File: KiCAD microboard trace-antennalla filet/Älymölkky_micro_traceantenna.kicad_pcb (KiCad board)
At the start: 2 copper layers, 57.2 x 21.1 mm, 43 parts, among them U1 nRF52810-QCxx, X1 32MHz Crystal, X1_C1 12pF, X1_C2 12pF, X2 32.768 kHz Crystal, X2_C11 12pF, X2_C12 12pF

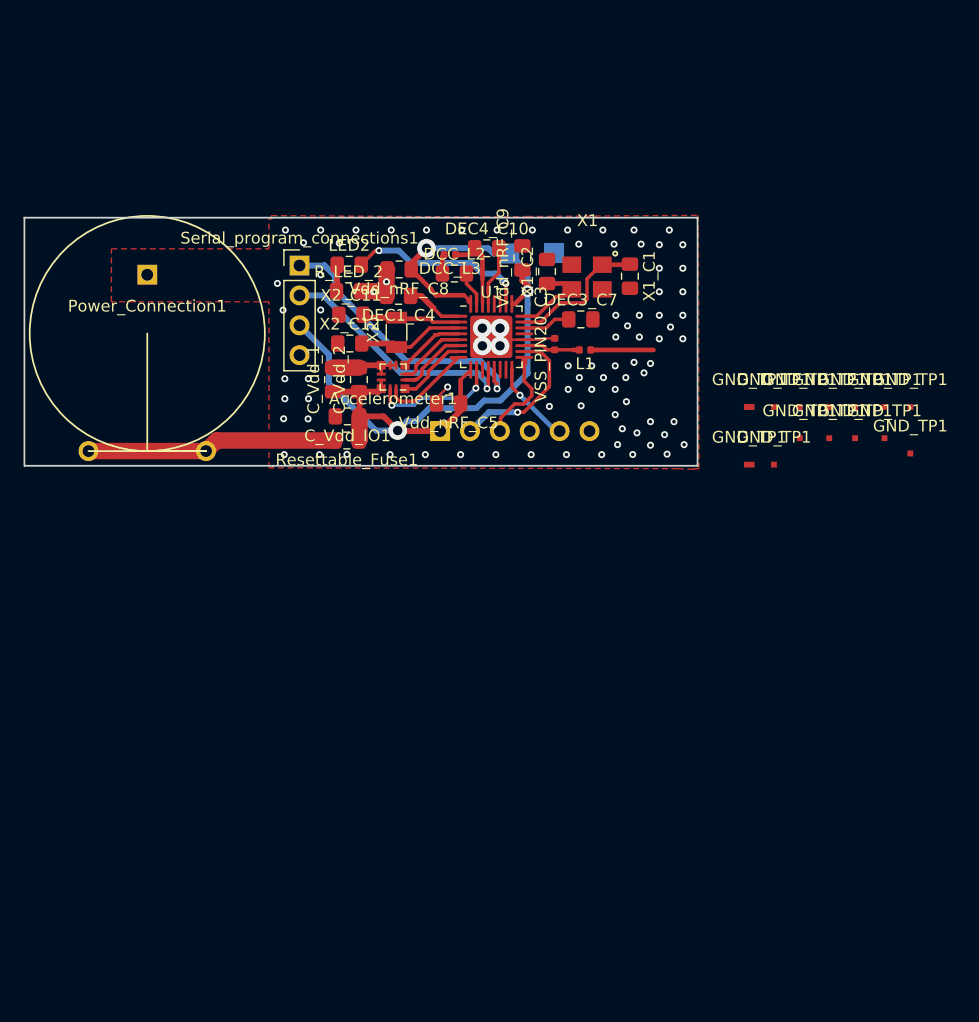
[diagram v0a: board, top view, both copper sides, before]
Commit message: Readymade design with antenna, only antenna connection not wide enough, needs 3mm
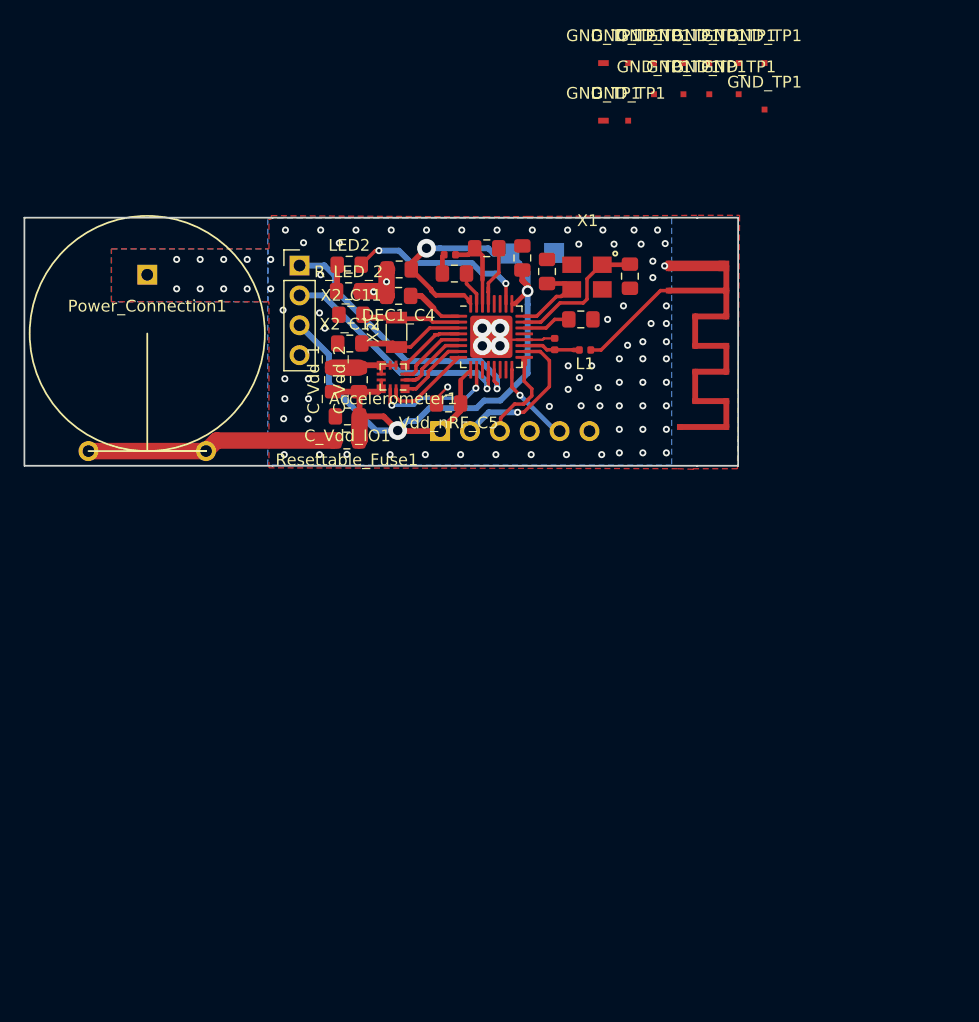
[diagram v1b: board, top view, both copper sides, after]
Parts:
- added ?: Conn_01x01_Male, Custom_footprints_alymolkky:antenna_building_block, F.Cu at (150.8, 92.2)
- added ?: Conn_01x01_Male, Custom_footprints_alymolkky:antenna_building_block, F.Cu at (148.2, 92.2)
- added ?: Conn_01x01_Male, Custom_footprints_alymolkky:antenna_building_block, F.Cu at (150.6, 88.0)
- added ?: Conn_01x01_Male, Custom_footprints_alymolkky:antenna_building_block, F.Cu at (150.8, 101.7)
- added ?: Conn_01x01_Male, Custom_footprints_alymolkky:antenna_building_block, F.Cu at (150.8, 90.0)
- added ?: Conn_01x01_Male, Custom_footprints_alymolkky:antenna_building_block, F.Cu at (148.2, 99.5)
- added ?: Conn_01x01_Male, Custom_footprints_alymolkky:antenna_building_block, F.Cu at (145.9, 88.0)
- added ?: Conn_01x01_Male, Custom_footprints_alymolkky:antenna_building_block, F.Cu at (148.2, 97.0)
- added ?: Conn_01x01_Male, Custom_footprints_alymolkky:antenna_building_block, F.Cu at (145.9, 90.0)
- added ?: Conn_01x01_Male, Custom_footprints_alymolkky:antenna_building_block, F.Cu at (150.8, 94.8)
- added ?: Conn_01x01_Male, Custom_footprints_alymolkky:antenna_building_block, F.Cu at (146.8, 101.7)
- added ?: Conn_01x01_Male, Custom_footprints_alymolkky:antenna_building_block, F.Cu at (150.8, 97.0)
- added ?: Conn_01x01_Male, Custom_footprints_alymolkky:antenna_building_block, F.Cu at (148.2, 94.8)
- added ?: Conn_01x01_Male, Custom_footprints_alymolkky:antenna_building_block, F.Cu at (150.8, 99.5)
- moved GND_TP1 31.8 mm to (140.3, 75.6)
- moved GND_TP1 31.8 mm to (149.3, 70.7)
- moved GND_TP1 31.8 mm to (147.2, 70.7)
- moved GND_TP1 31.8 mm to (147.2, 73.3)
- moved GND_TP1 31.8 mm to (144.7, 73.3)
- moved GND_TP1 31.8 mm to (144.7, 70.7)
- moved GND_TP1 31.8 mm to (140.3, 70.7)
- moved GND_TP1 31.8 mm to (142.4, 75.6)
- moved GND_TP1 31.8 mm to (142.4, 70.7)
- moved GND_TP1 31.8 mm to (151.8, 70.7)
- moved GND_TP1 31.8 mm to (151.8, 73.3)
- moved GND_TP1 31.8 mm to (149.3, 73.3)
- moved GND_TP1 31.8 mm to (154.1, 74.7)
- moved GND_TP1 31.8 mm to (154.1, 70.7)
- renumbered U1 to ?, DCC_L2 to ?, DEC3_C7 to ?, DEC4_C10 to ?, Vdd_nRF_C8 to ?, Vdd_nRF_C9 to ?, VSS_PIN20_C3 to ?, X1_C1 to ?, X1_C2 to ?, DCC_L3 to ?, Serial_program_connections1 to ?
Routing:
- net Earth: track 29.4 -> 70.7 mm, vias 86 -> 89
- added copper zone on B.Cu, net Earth
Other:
- board size 57.2 x 21.1 mm -> 60.7 x 21.1 mm
- board text added: "ÄlyMölkky"

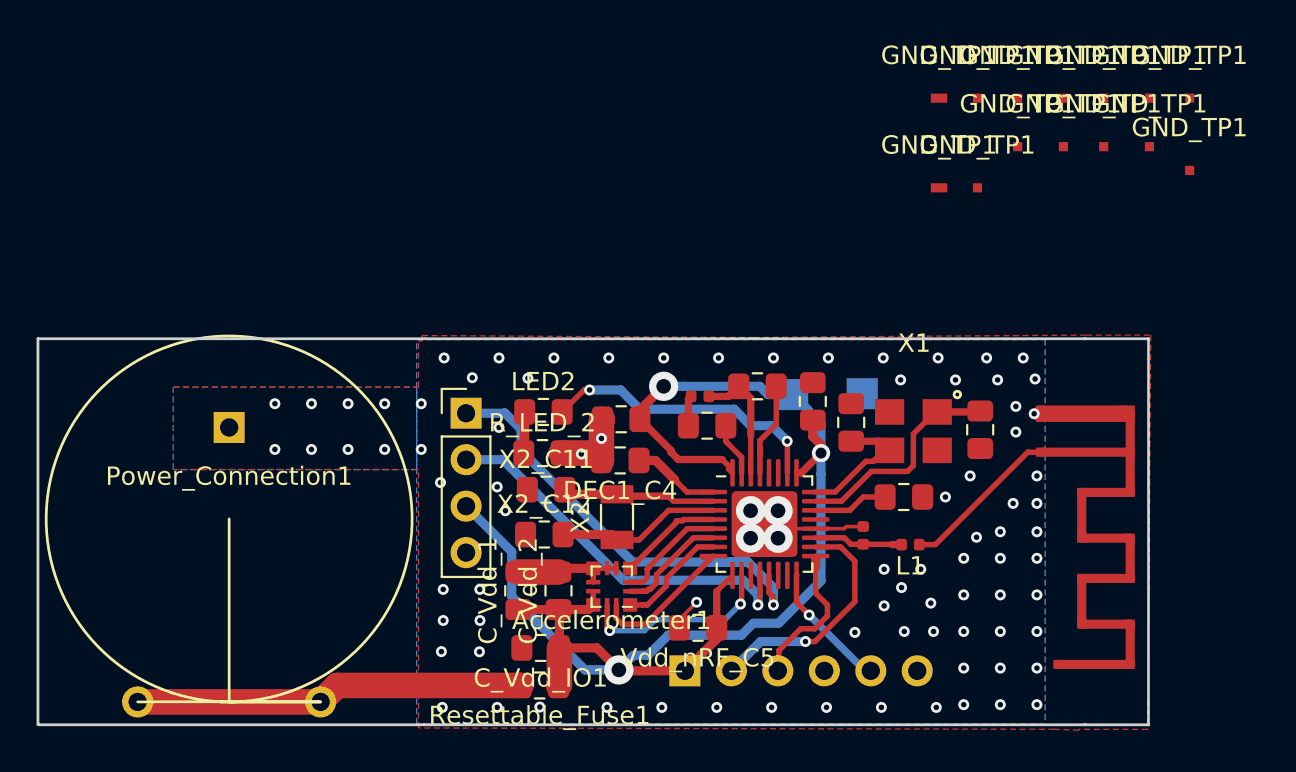
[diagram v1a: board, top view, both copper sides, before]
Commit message: Trace antenna design completed, modifying for order
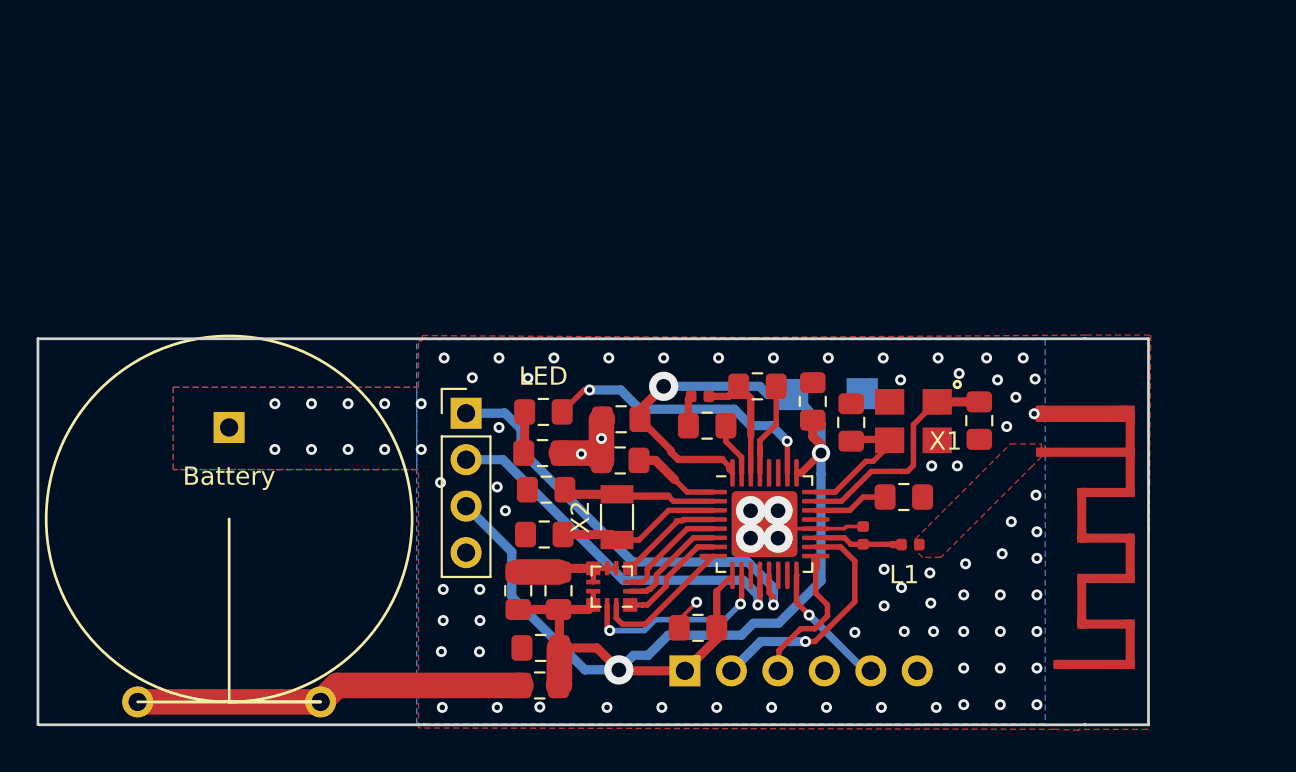
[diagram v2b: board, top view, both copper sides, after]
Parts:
- removed GND_TP1 (x14): Conn_01x01_Male, Custom_footprints_alymolkky:antenna_building_block
- moved X1 0.55 mm to (138.9, 88.3)
- moved ? 0.50 mm to (142.6, 88.3)
- renumbered SWD_connections1 to ?, Accelerometer1 to ?, C_Vdd_1 to ?, C_Vdd_2 to ?, C_Vdd_IO1 to ?, DEC1_C4 to ?, R_LED_2 to ?, Vdd_nRF_C5 to ?, Resettable_Fuse1 to ?, X2_C11 to ?, X2_C12 to ?, Power_Connection1 to Battery, GND_TP1 to GND_TP, LED2 to LED
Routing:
- net Earth: track 70.7 -> 62.0 mm, vias 89 -> 86
- net Net-(U1-Pad23): track 12.0 -> 12.5 mm
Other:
- board text added: "ÄlyMölkky v2.2 Micro with trace"
- board text removed: "ÄlyMölkky"

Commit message: Order ready trace antenna design
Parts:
- added ?: Conn_01x01_Male, Custom_footprints_alymolkky:antenna_building_block, F.Cu at (150.8, 139.8)
- added ?: Conn_01x01_Male, Custom_footprints_alymolkky:antenna_building_block, F.Cu at (150.8, 146.7)
- added ?: Conn_01x01_Male, Custom_footprints_alymolkky:antenna_building_block, F.Cu at (150.8, 135.1)
- added ?: Conn_01x01_Male, Custom_footprints_alymolkky:antenna_building_block, F.Cu at (148.2, 144.4)
- added ?: Conn_01x01_Male, Custom_footprints_alymolkky:antenna_building_block, F.Cu at (150.8, 141.9)
- added ?: Conn_01x01_Male, Custom_footprints_alymolkky:antenna_building_block, F.Cu at (146.8, 146.7)
- added ?: 100nF, Capacitor_SMD:C_0805_2012Metric_Pad1.15x1.40mm_HandSolder, F.Cu at (118.6, 145.8)
- added ?: 100uF, Capacitor_SMD:C_0805_2012Metric_Pad1.15x1.40mm_HandSolder, F.Cu at (117.3, 142.6)
- added ?: Conn_01x06_Male, Connector_PinHeader_2.54mm:PinHeader_1x06_P2.54mm_Vertical, B.Cu at (126.5, 147.0)
- added ?: LIS2DE12, Custom_footprints_alymolkky:LGA-12_2x2mm_P0.5mm, F.Cu at (122.5, 142.4)
- added ?: nRF52810-QCxx, Custom_footprints_alymolkky:QFN-32-1EP_5x5mm_P0.5mm_EP3.6x3.6mm, F.Cu at (130.8, 139.0)
- added ?: Conn_01x01_Male, Custom_footprints_alymolkky:antenna_building_block, F.Cu at (148.2, 137.2)
- added ?: 100nF, Capacitor_SMD:C_0805_2012Metric_Pad1.15x1.40mm_HandSolder, F.Cu at (122.9, 135.5)
- added ?: 10uH, Capacitor_SMD:C_0805_2012Metric_Pad1.15x1.40mm_HandSolder, F.Cu at (127.7, 133.6)
- added ?: 10uF, Capacitor_SMD:C_0805_2012Metric_Pad1.15x1.40mm_HandSolder, F.Cu at (119.5, 142.6)
- added ?: Polyfuse, Resistor_SMD:R_0805_2012Metric_Pad1.15x1.40mm_HandSolder, F.Cu at (118.5, 147.8)
- added ?: 100pF, Capacitor_SMD:C_0805_2012Metric_Pad1.15x1.40mm_HandSolder, F.Cu at (138.4, 137.5)
- added ?: 1.0uF, Capacitor_SMD:C_0805_2012Metric_Pad1.15x1.40mm_HandSolder, F.Cu at (130.4, 131.4)
- added ?: 12pF, Capacitor_SMD:C_0805_2012Metric_Pad1.15x1.40mm_HandSolder, F.Cu at (118.9, 137.1)
- added ?: 12pF, Capacitor_SMD:C_0805_2012Metric_Pad1.15x1.40mm_HandSolder, F.Cu at (118.8, 139.6)
- added ?: 15nH, Capacitor_SMD:C_0402_1005Metric, F.Cu at (127.3, 132.0)
- added ?: 12pF, Capacitor_SMD:C_0805_2012Metric_Pad1.15x1.40mm_HandSolder, F.Cu at (142.6, 133.3)
- added ?: Conn_01x01_Male, Custom_footprints_alymolkky:antenna_building_block, F.Cu at (150.6, 132.9)
- added ?: 12pF, Capacitor_SMD:C_0805_2012Metric_Pad1.15x1.40mm_HandSolder, F.Cu at (135.6, 133.4)
- added ?: 220, Resistor_SMD:R_0805_2012Metric_Pad1.15x1.40mm_HandSolder, F.Cu at (118.7, 135.1)
- added ?: 100nF, Capacitor_SMD:C_0805_2012Metric_Pad1.15x1.40mm_HandSolder, F.Cu at (127.2, 144.7)
- added ?: 100nF, Capacitor_SMD:C_0805_2012Metric_Pad1.15x1.40mm_HandSolder, F.Cu at (123.0, 133.2)
- added ?: Conn_01x04_Male, Connector_PinHeader_2.54mm:PinHeader_1x04_P2.54mm_Vertical, F.Cu at (114.5, 132.9)
- added ?: 4.7uF, Capacitor_SMD:C_0805_2012Metric_Pad1.15x1.40mm_HandSolder, F.Cu at (133.4, 132.3)
- added ?: 0.8pF, Capacitor_SMD:C_0402_1005Metric, F.Cu at (136.2, 139.6)
- added ?: 100nF, Capacitor_SMD:C_0805_2012Metric_Pad1.15x1.40mm_HandSolder, F.Cu at (123.0, 110.8)
- added ?: 100nF, Capacitor_SMD:C_0805_2012Metric_Pad1.15x1.40mm_HandSolder, F.Cu at (127.2, 122.2)
- added ?: 220, Resistor_SMD:R_0805_2012Metric_Pad1.15x1.40mm_HandSolder, F.Cu at (118.7, 112.6)
- added ?: Conn_01x01_Male, Custom_footprints_alymolkky:antenna_building_block, F.Cu at (148.2, 139.8)
- added ?: 12pF, Capacitor_SMD:C_0805_2012Metric_Pad1.15x1.40mm_HandSolder, F.Cu at (142.6, 110.8)
- added ?: Polyfuse, Resistor_SMD:R_0805_2012Metric_Pad1.15x1.40mm_HandSolder, F.Cu at (118.5, 125.3)
- added ?: 12pF, Capacitor_SMD:C_0805_2012Metric_Pad1.15x1.40mm_HandSolder, F.Cu at (135.6, 110.9)
- added ?: 15nH, Capacitor_SMD:C_0402_1005Metric, F.Cu at (127.3, 109.5)
- added ?: Conn_01x04_Male, Connector_PinHeader_2.54mm:PinHeader_1x04_P2.54mm_Vertical, F.Cu at (114.5, 110.4)
- added ?: 4.7uF, Capacitor_SMD:C_0805_2012Metric_Pad1.15x1.40mm_HandSolder, F.Cu at (133.4, 109.8)
- added ?: 12pF, Capacitor_SMD:C_0805_2012Metric_Pad1.15x1.40mm_HandSolder, F.Cu at (118.8, 117.0)
- added ?: 12pF, Capacitor_SMD:C_0805_2012Metric_Pad1.15x1.40mm_HandSolder, F.Cu at (118.9, 114.6)
- added ?: 0.8pF, Capacitor_SMD:C_0402_1005Metric, F.Cu at (136.2, 117.1)
- added ?: 100pF, Capacitor_SMD:C_0805_2012Metric_Pad1.15x1.40mm_HandSolder, F.Cu at (138.4, 115.0)
- added ?: Conn_01x01_Male, Custom_footprints_alymolkky:antenna_building_block, F.Cu at (145.9, 132.9)
- added ?: 1.0uF, Capacitor_SMD:C_0805_2012Metric_Pad1.15x1.40mm_HandSolder, F.Cu at (130.4, 109.0)
- added ?: nRF52810-QCxx, Custom_footprints_alymolkky:QFN-32-1EP_5x5mm_P0.5mm_EP3.6x3.6mm, F.Cu at (130.8, 116.5)
- added ?: 100nF, Capacitor_SMD:C_0805_2012Metric_Pad1.15x1.40mm_HandSolder, F.Cu at (122.9, 113.0)
- added ?: LIS2DE12, Custom_footprints_alymolkky:LGA-12_2x2mm_P0.5mm, F.Cu at (122.5, 119.9)
- added ?: 10uH, Capacitor_SMD:C_0805_2012Metric_Pad1.15x1.40mm_HandSolder, F.Cu at (127.7, 111.1)
- added ?: 10uF, Capacitor_SMD:C_0805_2012Metric_Pad1.15x1.40mm_HandSolder, F.Cu at (119.5, 120.1)
- added ?: 100nF, Capacitor_SMD:C_0805_2012Metric_Pad1.15x1.40mm_HandSolder, F.Cu at (118.6, 123.2)
- added ?: 100uF, Capacitor_SMD:C_0805_2012Metric_Pad1.15x1.40mm_HandSolder, F.Cu at (117.3, 120.1)
- added ?: Conn_01x06_Male, Connector_PinHeader_2.54mm:PinHeader_1x06_P2.54mm_Vertical, B.Cu at (126.5, 124.5)
- added ?: Conn_01x01_Male, Custom_footprints_alymolkky:antenna_building_block, F.Cu at (146.8, 124.2)
- added ?: Conn_01x01_Male, Custom_footprints_alymolkky:antenna_building_block, F.Cu at (150.8, 137.2)
- added ?: Conn_01x01_Male, Custom_footprints_alymolkky:antenna_building_block, F.Cu at (148.2, 119.5)
- added ?: Conn_01x01_Male, Custom_footprints_alymolkky:antenna_building_block, F.Cu at (150.8, 114.8)
- added ?: Conn_01x01_Male, Custom_footprints_alymolkky:antenna_building_block, F.Cu at (145.9, 110.5)
- added ?: Conn_01x01_Male, Custom_footprints_alymolkky:antenna_building_block, F.Cu at (145.9, 112.5)
- added ?: Conn_01x01_Male, Custom_footprints_alymolkky:antenna_building_block, F.Cu at (150.8, 117.2)
- added ?: Conn_01x01_Male, Custom_footprints_alymolkky:antenna_building_block, F.Cu at (148.2, 117.2)
- added ?: Conn_01x01_Male, Custom_footprints_alymolkky:antenna_building_block, F.Cu at (150.8, 122.0)
- added ?: Conn_01x01_Male, Custom_footprints_alymolkky:antenna_building_block, F.Cu at (148.2, 114.8)
- added ?: Conn_01x01_Male, Custom_footprints_alymolkky:antenna_building_block, F.Cu at (150.6, 110.5)
- added ?: Conn_01x01_Male, Custom_footprints_alymolkky:antenna_building_block, F.Cu at (150.8, 124.2)
- added ?: Conn_01x01_Male, Custom_footprints_alymolkky:antenna_building_block, F.Cu at (150.8, 144.4)
- added ?: Conn_01x01_Male, Custom_footprints_alymolkky:antenna_building_block, F.Cu at (150.8, 112.5)
- added ?: Conn_01x01_Male, Custom_footprints_alymolkky:antenna_building_block, F.Cu at (148.2, 122.0)
- added ?: Conn_01x01_Male, Custom_footprints_alymolkky:antenna_building_block, F.Cu at (150.8, 119.5)
- added ?: Conn_01x01_Male, Custom_footprints_alymolkky:antenna_building_block, F.Cu at (148.2, 141.9)
- added ?: Conn_01x01_Male, Custom_footprints_alymolkky:antenna_building_block, F.Cu at (145.9, 135.1)
- added Battery: Conn_01x02_Female, Custom_footprints_alymolkky:PinHeader_1x02_P2.54mm_Vertical, F.Cu at (101.5, 138.7)
- added Battery: Conn_01x02_Female, Custom_footprints_alymolkky:PinHeader_1x02_P2.54mm_Vertical, F.Cu at (101.5, 116.2)
- added GND_TP: Conn_01x01_Male, Connector_PinHeader_2.54mm:PinHeader_1x01_P2.54mm_Vertical, B.Cu at (136.2, 131.8)
- added GND_TP: Conn_01x01_Male, Connector_PinHeader_2.54mm:PinHeader_1x01_P2.54mm_Vertical, B.Cu at (136.2, 109.3)
- added L1: 3.9nH, Resistor_SMD:R_0402_1005Metric, F.Cu at (138.8, 140.1)
- added L1: 3.9nH, Resistor_SMD:R_0402_1005Metric, F.Cu at (138.8, 117.6)
- added LED: LED_ALT, Resistor_SMD:R_0805_2012Metric_Pad1.15x1.40mm_HandSolder, F.Cu at (118.7, 132.8)
- added LED: LED_ALT, Resistor_SMD:R_0805_2012Metric_Pad1.15x1.40mm_HandSolder, F.Cu at (118.7, 110.3)
- added VDD_TP1: Conn_01x01_Male, Connector_PinHeader_2.54mm:PinHeader_1x01_P2.54mm_Vertical, B.Cu at (132.3, 131.9)
- added VDD_TP1: Conn_01x01_Male, Connector_PinHeader_2.54mm:PinHeader_1x01_P2.54mm_Vertical, B.Cu at (132.3, 109.4)
- added X1: 32MHz Crystal, Custom_footprints_alymolkky:Crystal_3.2x2.5x0.8, F.Cu at (138.9, 133.3)
- added X1: 32MHz Crystal, Custom_footprints_alymolkky:Crystal_3.2x2.5x0.8, F.Cu at (138.9, 110.8)
- added X2: 32.768 kHz Crystal, Crystal:Crystal_SMD_3215-2Pin_3.2x1.5mm, F.Cu at (122.8, 138.6)
- added X2: 32.768 kHz Crystal, Crystal:Crystal_SMD_3215-2Pin_3.2x1.5mm, F.Cu at (122.8, 116.1)
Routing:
- net VDD: track 80.3 -> 241.0 mm, vias 3 -> 9
- net Earth: track 62.0 -> 185.9 mm, vias 86 -> 258
- net /~TX0: track 26.5 -> 79.4 mm, vias 1 -> 3
- net Net-(Power_Connection1-Pad2): track 21.3 -> 64.0 mm
- net /~RX1: track 21.2 -> 63.6 mm, vias 1 -> 3
- net Net-(LED2-Pad2): track 15.7 -> 47.1 mm, vias 2 -> 6
- net /~SWDIO: track 13.0 -> 39.0 mm, vias 1 -> 3
- net Net-(U1-Pad23): track 12.5 -> 37.4 mm
- net /~INT2: track 11.0 -> 33.0 mm, vias 2 -> 6
- net Net-(U1-Pad3): track 9.41 -> 28.2 mm
- net /~SWDCLK: track 8.33 -> 25.0 mm
- net /~INT1: track 8.30 -> 24.9 mm
- net Net-(U1-Pad2): track 8.08 -> 24.2 mm
- net Net-(U1-Pad24): track 7.54 -> 22.6 mm
- net /~Reset: track 7.11 -> 21.3 mm, vias 1 -> 3
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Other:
- board size 60.7 x 21.1 mm -> 60.7 x 66.1 mm
